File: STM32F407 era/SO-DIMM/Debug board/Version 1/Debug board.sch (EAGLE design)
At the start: 16 parts, among them J4 FTDI_DEVICE, J8 22-27-2021-02, X1 057-014-1, X2 BN35N61, X3 BN35N61, X4 BN35N61, X5 BN35N61, X6 BN35N61

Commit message: All board V1-RC1 done
all boards ready for inspection
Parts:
- added U$21: MICROFIT4, unicorn:MICROFIT4
- added U5, U6: (no value), connector:AUDIO-JACKPTH
- added X7, X8: BN35N61, con-coax:BN35N61
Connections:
- net CAN_N: now also U$21.PIN2, U5.LEFT, U6.LEFT, X7G$1.1
- net CAN_P: now also U$21.PIN1, U5.RIGHT, U6.RIGHT, X8G$1.1
- net GND: now also U$21.PIN3, U$21.PIN4, U5.SLEEVE, U6.SLEEVE, X7G$1.GND, X8G$1.GND
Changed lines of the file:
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@@
 <layer number="59" name="tCarbon" color="7" fill="1" visible="no" active="no"/>
 <layer number="60" name="bCarbon" color="7" fill="1" visible="no" active="no"/>
+<layer number="61" name="stand" color="7" fill="1" visible="no" active="no"/>
 <layer number="90" name="Modules" color="5" fill="1" visible="yes" active="yes"/>
 <layer number="91" name="Nets" color="2" fill="1" visible="yes" active="yes"/>
@@
 <layer number="128" name="_bValues" color="7" fill="1" visible="yes" active="yes"/>
 <layer number="129" name="Mask" color="7" fill="1" visible="yes" active="yes"/>
+<layer number="130" name="bLogo" color="7" fill="1" visible="yes" active="yes"/>
 <layer number="131" name="tAdjust" color="7" fill="1" visible="yes" active="yes"/>
 <layer number="132" name="bAdjust" color="7" fill="1" visible="yes" active="yes"/>
@@
 <part name="U$4" library="microbuilder" deviceset="12V" device=""/>
 <part name="GND10" library="supply1" deviceset="GND" device=""/>
+<part name="U5" library="connector" deviceset="AUDIO-JACK" device="PTH"/>
+<part name="U6" library="connector" deviceset="AUDIO-JACK" device="PTH"/>
+<part name="GND17" library="supply1" deviceset="GND" device=""/>
+<part name="U$21" library="unicorn" deviceset="MICROFIT4" device=""/>
+<part name="U$24" library="microbuilder" deviceset="GND" device=""/>
+<part name="X7" library="con-coax" deviceset="BN35N61" device=""/>
+<part name="X8" library="con-coax" deviceset="BN35N61" device=""/>
+<part name="GND11" library="supply1" deviceset="GND" device=""/>
+<part name="GND12" library="supply1" deviceset="GND" device=""/>
 </parts>
 <sheets>
@@
 <wire x1="96.52" y1="175.26" x2="96.52" y2="170.18" width="0.3048" layer="97"/>
 <wire x1="96.52" y1="170.18" x2="96.52" y2="134.62" width="0.3048" layer="97"/>
-<wire x1="96.52" y1="134.62" x2="160.02" y2="134.62" width="0.3048" layer="97"/>
-<wire x1="160.02" y1="134.62" x2="160.02" y2="175.26" width="0.3048" layer="97"/>
-<wire x1="160.02" y1="175.26" x2="132.08" y2="175.26" width="0.3048" layer="97"/>
+<wire x1="96.52" y1="134.62" x2="185.42" y2="134.62" width="0.3048" layer="97"/>
+<wire x1="185.42" y1="134.62" x2="185.42" y2="175.26" width="0.3048" layer="97"/>
+<wire x1="185.42" y1="175.26" x2="132.08" y2="175.26" width="0.3048" layer="97"/>
 <text x="99.06" y="172.72" size="1.778" layer="97" font="vector">BNC signal headers</text>
 <wire x1="132.08" y1="175.26" x2="96.52" y2="175.26" width="0.3048" layer="97"/>
@@
 <instance part="U$4" gate="G$1" x="114.3" y="119.38"/>
 <instance part="GND10" gate="1" x="114.3" y="104.14"/>
+<instance part="U5" gate="G$1" x="160.02" y="119.38"/>
+<instance part="U6" gate="G$1" x="160.02" y="111.76"/>
+<instance part="GND17" gate="1" x="167.64" y="104.14"/>
+<instance part="U$21" gate="G$1" x="177.8" y="91.44"/>
+<instance part="U$24" gate="G$1" x="167.64" y="83.82"/>
+<instance part="X7" gate="G$1" x="152.4" y="147.32" rot="MR0"/>
+<instance part="X8" gate="G$1" x="172.72" y="165.1" rot="MR0"/>
+<instance part="GND11" gate="1" x="147.32" y="139.7"/>
+<instance part="GND12" gate="1" x="167.64" y="157.48"/>
 </instances>
 <busses>
@@
 <wire x1="114.3" y1="109.22" x2="114.3" y2="106.68" width="0.1524" layer="91"/>
 </segment>
+<segment>
+<pinref part="U6" gate="G$1" pin="SLEEVE"/>
+<wire x1="165.1" y1="114.3" x2="167.64" y2="114.3" width="0.1524" layer="91"/>
+<wire x1="167.64" y1="114.3" x2="167.64" y2="106.68" width="0.1524" layer="91"/>
+<pinref part="U5" gate="G$1" pin="SLEEVE"/>
+<wire x1="165.1" y1="121.92" x2="167.64" y2="121.92" width="0.1524" layer="91"/>
+<wire x1="167.64" y1="121.92" x2="167.64" y2="114.3" width="0.1524" layer="91"/>
+<junction x="167.64" y="114.3"/>
+<pinref part="GND17" gate="1" pin="GND"/>
+</segment>
+<segment>
+<pinref part="U$21" gate="G$1" pin="PIN3"/>
+<pinref part="U$24" gate="G$1" pin="GND"/>
+<wire x1="170.18" y1="91.44" x2="167.64" y2="91.44" width="0.1524" layer="91"/>
+<wire x1="167.64" y1="91.44" x2="167.64" y2="88.9" width="0.1524" layer="91"/>
+<pinref part="U$21" gate="G$1" pin="PIN4"/>
+<wire x1="167.64" y1="88.9" x2="167.64" y2="86.36" width="0.1524" layer="91"/>
+<wire x1="170.18" y1="88.9" x2="167.64" y2="88.9" width="0.1524" layer="91"/>
+<junction x="167.64" y="88.9"/>
+</segment>
+<segment>
+<pinref part="X7" gate="G$1" pin="GND"/>
+<pinref part="GND11" gate="1" pin="GND"/>
+<wire x1="149.86" y1="144.78" x2="147.32" y2="144.78" width="0.1524" layer="91"/>
+<wire x1="147.32" y1="144.78" x2="147.32" y2="142.24" width="0.1524" layer="91"/>
+</segment>
+<segment>
+<pinref part="X8" gate="G$1" pin="GND"/>
+<pinref part="GND12" gate="1" pin="GND"/>
+<wire x1="170.18" y1="162.56" x2="167.64" y2="162.56" width="0.1524" layer="91"/>
+<wire x1="167.64" y1="162.56" x2="167.64" y2="160.02" width="0.1524" layer="91"/>
+</segment>
 </net>
 <net name="3.3V" class="0">
@@
 <label x="81.28" y="109.22" size="1.27" layer="95" rot="R180" xref="yes"/>
 </segment>
+<segment>
+<pinref part="U6" gate="G$1" pin="RIGHT"/>
+<wire x1="165.1" y1="111.76" x2="170.18" y2="111.76" width="0.1524" layer="91"/>
+<pinref part="U5" gate="G$1" pin="RIGHT"/>
+<wire x1="165.1" y1="119.38" x2="170.18" y2="119.38" width="0.1524" layer="91"/>
+<wire x1="170.18" y1="119.38" x2="175.26" y2="119.38" width="0.1524" layer="91"/>
+<wire x1="170.18" y1="111.76" x2="170.18" y2="119.38" width="0.1524" layer="91"/>
+<junction x="170.18" y="119.38"/>
+<label x="175.26" y="119.38" size="1.27" layer="95" xref="yes"/>
+</segment>
+<segment>
+<pinref part="U$21" gate="G$1" pin="PIN1"/>
+<wire x1="170.18" y1="96.52" x2="167.64" y2="96.52" width="0.1524" layer="91"/>
+<label x="167.64" y="96.52" size="1.27" layer="95" rot="R180" xref="yes"/>
+</segment>
+<segment>
+<pinref part="X8" gate="G$1" pin="1"/>
+<wire x1="167.64" y1="165.1" x2="170.18" y2="165.1" width="0.1524" layer="91"/>
+<label x="167.64" y="165.1" size="1.27" layer="95" rot="R180" xref="yes"/>
+</segment>
 </net>
 <net name="CAN_N" class="0">
@@
 <label x="81.28" y="119.38" size="1.27" layer="95" rot="R180" xref="yes"/>
 </segment>
+<segment>
+<pinref part="U6" gate="G$1" pin="LEFT"/>
+<wire x1="165.1" y1="109.22" x2="172.72" y2="109.22" width="0.1524" layer="91"/>
+<pinref part="U5" gate="G$1" pin="LEFT"/>
+<wire x1="165.1" y1="116.84" x2="172.72" y2="116.84" width="0.1524" layer="91"/>
+<wire x1="172.72" y1="116.84" x2="175.26" y2="116.84" width="0.1524" layer="91"/>
+<wire x1="172.72" y1="109.22" x2="172.72" y2="116.84" width="0.1524" layer="91"/>
+<junction x="172.72" y="116.84"/>
+<label x="175.26" y="116.84" size="1.27" layer="95" xref="yes"/>
+</segment>
+<segment>
+<pinref part="U$21" gate="G$1" pin="PIN2"/>
+<wire x1="170.18" y1="93.98" x2="167.64" y2="93.98" width="0.1524" layer="91"/>
+<label x="167.64" y="93.98" size="1.27" layer="95" rot="R180" xref="yes"/>
+</segment>
+<segment>
+<pinref part="X7" gate="G$1" pin="1"/>
+<wire x1="147.32" y1="147.32" x2="149.86" y2="147.32" width="0.1524" layer="91"/>
+<label x="147.32" y="147.32" size="1.27" layer="95" rot="R180" xref="yes"/>
+</segment>
 </net>

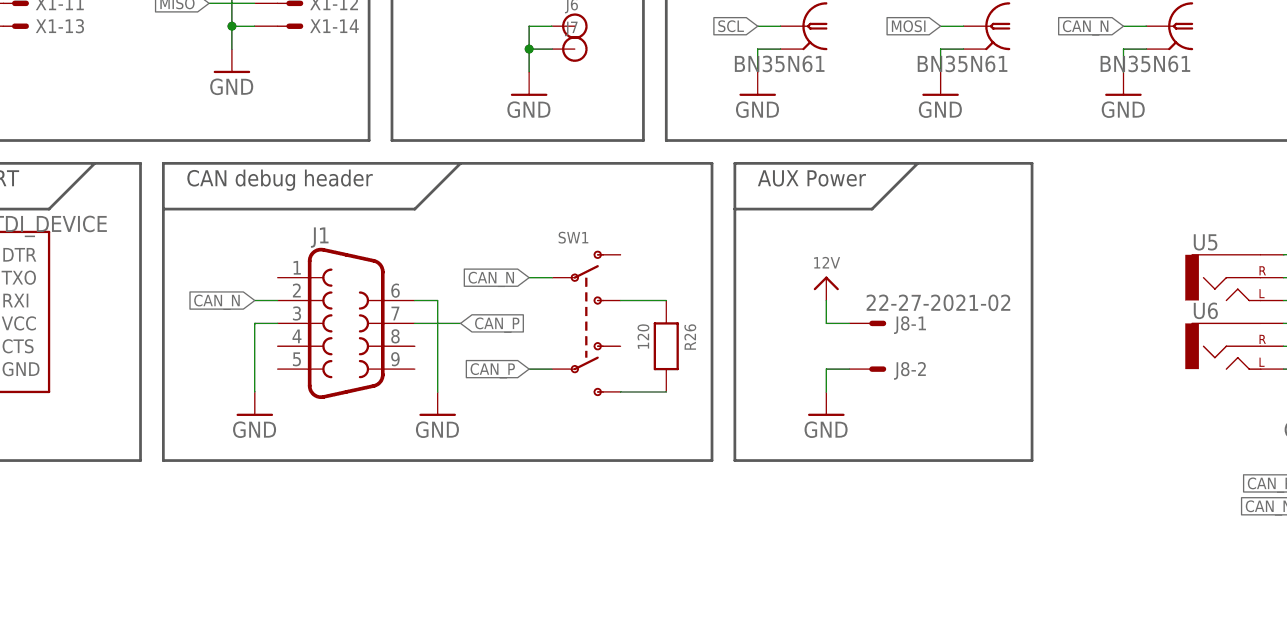
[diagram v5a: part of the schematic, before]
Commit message: last end changes on boards
Dev board
- Added 8 LED for ekstra debugging feature
- fixed Tvalue silkscreen
-

COM/TC
- fixed connections om P-channel RPP
- 12V from debug changed to include RPP and fuse

Dash
- fixed connections om P-channel RPP
- 12V from debug changed to include RPP and fuse

debug
- Added "ohm/not ohm to silkscreen
- Added BNC connectors for CAN

and much much more
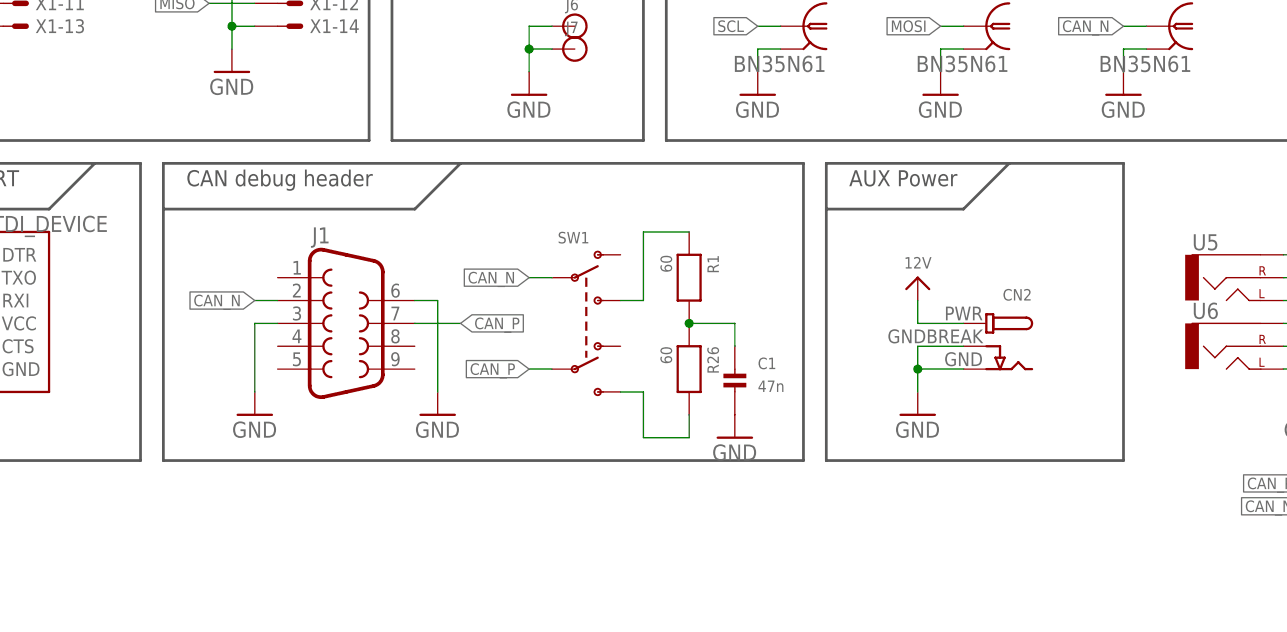
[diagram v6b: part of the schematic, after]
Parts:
- removed J8: 22-27-2021-02, con-molex:22-27-2021-02
- added C1: 47n, microbuilder:CAP_CERAMIC_0603
- added CN2: (no value), microbuilder:DCBARRELPTH
- added R1: 60, microbuilder:RESISTOR_0603
- R26: value 120 -> 60
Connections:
- removed net N$8: R26.1, SW1.S1
- new net N$1: C1.P$1, R1.2, R26.1
- new net N$2: R1.1, SW1.S1
- net 12V: now also CN2.PWR; no longer J8-1.S
- net GND: now also C1.P$2, CN2.GND, CN2.GNDBREAK; no longer J8-2.S
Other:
- moved on the sheet: R26
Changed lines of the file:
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@@
 <part name="GND7" library="supply1" deviceset="GND" device=""/>
 <part name="SW1" library="microbuilder" deviceset="SWITCH_DPDT" device=""/>
-<part name="R26" library="microbuilder" deviceset="RESISTOR" device="_0603" value="120"/>
+<part name="R26" library="microbuilder" deviceset="RESISTOR" device="_0603" value="60"/>
 <part name="X2" library="con-coax" deviceset="BN35N61" device=""/>
 <part name="X3" library="con-coax" deviceset="BN35N61" device=""/>
@@
 <part name="J7" library="SparkFun-Connectors" deviceset="BANANA_CONN" device=""/>
 <part name="FRAME1" library="SparkFun-Aesthetics" deviceset="FRAME-A4L" device=""/>
-<part name="J8" library="con-molex" deviceset="22-?-02" device="27-2021"/>
 <part name="U$4" library="microbuilder" deviceset="12V" device=""/>
 <part name="GND10" library="supply1" deviceset="GND" device=""/>
@@
 <part name="GND11" library="supply1" deviceset="GND" device=""/>
 <part name="GND12" library="supply1" deviceset="GND" device=""/>
+<part name="R1" library="microbuilder" deviceset="RESISTOR" device="_0603" value="60"/>
+<part name="C1" library="microbuilder" deviceset="CAP_CERAMIC" device="_0603" value="47n"/>
+<part name="GND13" library="supply1" deviceset="GND" device=""/>
+<part name="CN2" library="microbuilder" deviceset="DCBARREL" device="PTH"/>
 </parts>
 <sheets>
@@
 <wire x1="40.64" y1="132.08" x2="40.64" y2="127" width="0.3048" layer="97"/>
 <wire x1="40.64" y1="127" x2="40.64" y2="99.06" width="0.3048" layer="97"/>
-<wire x1="40.64" y1="99.06" x2="101.6" y2="99.06" width="0.3048" layer="97"/>
-<wire x1="101.6" y1="99.06" x2="101.6" y2="132.08" width="0.3048" layer="97"/>
-<wire x1="101.6" y1="132.08" x2="73.66" y2="132.08" width="0.3048" layer="97"/>
+<wire x1="40.64" y1="99.06" x2="111.76" y2="99.06" width="0.3048" layer="97"/>
+<wire x1="111.76" y1="99.06" x2="111.76" y2="132.08" width="0.3048" layer="97"/>
+<wire x1="111.76" y1="132.08" x2="73.66" y2="132.08" width="0.3048" layer="97"/>
 <text x="43.18" y="129.54" size="1.778" layer="97" font="vector">CAN debug header</text>
 <wire x1="73.66" y1="132.08" x2="40.64" y2="132.08" width="0.3048" layer="97"/>
@@
 <wire x1="96.52" y1="170.18" x2="127" y2="170.18" width="0.3048" layer="97"/>
 <wire x1="127" y1="170.18" x2="132.08" y2="175.26" width="0.3048" layer="97"/>
-<wire x1="104.14" y1="132.08" x2="124.46" y2="132.08" width="0.3048" layer="97"/>
-<wire x1="124.46" y1="132.08" x2="137.16" y2="132.08" width="0.3048" layer="97"/>
-<wire x1="137.16" y1="132.08" x2="137.16" y2="99.06" width="0.3048" layer="97"/>
-<wire x1="137.16" y1="99.06" x2="104.14" y2="99.06" width="0.3048" layer="97"/>
-<wire x1="104.14" y1="99.06" x2="104.14" y2="127" width="0.3048" layer="97"/>
-<text x="106.68" y="129.54" size="1.778" layer="97" font="vector">AUX Power</text>
-<wire x1="104.14" y1="127" x2="104.14" y2="132.08" width="0.3048" layer="97"/>
-<wire x1="104.14" y1="127" x2="119.38" y2="127" width="0.3048" layer="97"/>
-<wire x1="119.38" y1="127" x2="124.46" y2="132.08" width="0.3048" layer="97"/>
+<wire x1="114.3" y1="132.08" x2="134.62" y2="132.08" width="0.3048" layer="97"/>
+<wire x1="134.62" y1="132.08" x2="147.32" y2="132.08" width="0.3048" layer="97"/>
+<wire x1="147.32" y1="132.08" x2="147.32" y2="99.06" width="0.3048" layer="97"/>
+<wire x1="147.32" y1="99.06" x2="114.3" y2="99.06" width="0.3048" layer="97"/>
+<wire x1="114.3" y1="99.06" x2="114.3" y2="127" width="0.3048" layer="97"/>
+<text x="116.84" y="129.54" size="1.778" layer="97" font="vector">AUX Power</text>
+<wire x1="114.3" y1="127" x2="114.3" y2="132.08" width="0.3048" layer="97"/>
+<wire x1="114.3" y1="127" x2="129.54" y2="127" width="0.3048" layer="97"/>
+<wire x1="129.54" y1="127" x2="134.62" y2="132.08" width="0.3048" layer="97"/>
 </plain>
 <instances>
@@
 <instance part="GND7" gate="1" x="71.12" y="104.14"/>
 <instance part="SW1" gate="G$1" x="88.9" y="114.3"/>
-<instance part="R26" gate="G$1" x="96.52" y="111.76" rot="R270"/>
+<instance part="R26" gate="G$1" x="99.06" y="109.22" rot="R270"/>
 <instance part="X2" gate="G$1" x="111.76" y="165.1" rot="MR0"/>
 <instance part="X3" gate="G$1" x="132.08" y="165.1" rot="MR0"/>
@@
 <instance part="J7" gate="G$1" x="86.36" y="144.78"/>
 <instance part="FRAME1" gate="G$1" x="0" y="0"/>
-<instance part="J8" gate="-1" x="119.38" y="114.3"/>
-<instance part="J8" gate="-2" x="119.38" y="109.22"/>
-<instance part="U$4" gate="G$1" x="114.3" y="119.38"/>
-<instance part="GND10" gate="1" x="114.3" y="104.14"/>
+<instance part="U$4" gate="G$1" x="124.46" y="119.38"/>
+<instance part="GND10" gate="1" x="124.46" y="104.14"/>
 <instance part="U5" gate="G$1" x="160.02" y="119.38"/>
 <instance part="U6" gate="G$1" x="160.02" y="111.76"/>
@@
 <instance part="GND11" gate="1" x="147.32" y="139.7"/>
 <instance part="GND12" gate="1" x="167.64" y="157.48"/>
+<instance part="R1" gate="G$1" x="99.06" y="119.38" rot="R270"/>
+<instance part="C1" gate="G$1" x="104.14" y="106.68"/>
+<instance part="GND13" gate="1" x="104.14" y="101.6"/>
+<instance part="CN2" gate="G$1" x="132.08" y="111.76" rot="MR0"/>
 </instances>
 <busses>
@@
 </segment>
 <segment>
-<pinref part="J8" gate="-2" pin="S"/>
 <pinref part="GND10" gate="1" pin="GND"/>
-<wire x1="116.84" y1="109.22" x2="114.3" y2="109.22" width="0.1524" layer="91"/>
-<wire x1="114.3" y1="109.22" x2="114.3" y2="106.68" width="0.1524" layer="91"/>
+<wire x1="129.54" y1="109.22" x2="124.46" y2="109.22" width="0.1524" layer="91"/>
+<wire x1="124.46" y1="109.22" x2="124.46" y2="106.68" width="0.1524" layer="91"/>
+<pinref part="CN2" gate="G$1" pin="GND"/>
+<pinref part="CN2" gate="G$1" pin="GNDBREAK"/>
+<wire x1="129.54" y1="111.76" x2="124.46" y2="111.76" width="0.1524" layer="91"/>
+<wire x1="124.46" y1="111.76" x2="124.46" y2="109.22" width="0.1524" layer="91"/>
+<junction x="124.46" y="109.22"/>
 </segment>
 <segment>
@@
 <wire x1="167.64" y1="162.56" x2="167.64" y2="160.02" width="0.1524" layer="91"/>
 </segment>
+<segment>
+<pinref part="C1" gate="G$1" pin="P$2"/>
+<pinref part="GND13" gate="1" pin="GND"/>
+</segment>
 </net>
 <net name="3.3V" class="0">
@@
 </segment>
 <segment>
-<pinref part="J8" gate="-1" pin="S"/>
 <pinref part="U$4" gate="G$1" pin="12V"/>
-<wire x1="116.84" y1="114.3" x2="114.3" y2="114.3" width="0.1524" layer="91"/>
-<wire x1="114.3" y1="114.3" x2="114.3" y2="116.84" width="0.1524" layer="91"/>
+<wire x1="129.54" y1="114.3" x2="124.46" y2="114.3" width="0.1524" layer="91"/>
+<wire x1="124.46" y1="114.3" x2="124.46" y2="116.84" width="0.1524" layer="91"/>
+<pinref part="CN2" gate="G$1" pin="PWR"/>
 </segment>
 </net>
@@
 <pinref part="SW1" gate="G$1" pin="S2"/>
 <pinref part="R26" gate="G$1" pin="2"/>
-<wire x1="91.44" y1="106.68" x2="96.52" y2="106.68" width="0.1524" layer="91"/>
-</segment>
-</net>
-<net name="N$8" class="0">
-<segment>
+<wire x1="91.44" y1="106.68" x2="93.98" y2="106.68" width="0.1524" layer="91"/>
+<wire x1="93.98" y1="106.68" x2="93.98" y2="101.6" width="0.1524" layer="91"/>
+<wire x1="93.98" y1="101.6" x2="99.06" y2="101.6" width="0.1524" layer="91"/>
+<wire x1="99.06" y1="101.6" x2="99.06" y2="104.14" width="0.1524" layer="91"/>
+</segment>
+</net>
+<net name="N$1" class="0">
+<segment>
+<pinref part="R26" gate="G$1" pin="1"/>
+<pinref part="R1" gate="G$1" pin="2"/>
+<pinref part="C1" gate="G$1" pin="P$1"/>
+<wire x1="99.06" y1="114.3" x2="104.14" y2="114.3" width="0.1524" layer="91"/>
+<wire x1="104.14" y1="114.3" x2="104.14" y2="111.76" width="0.1524" layer="91"/>
+<junction x="99.06" y="114.3"/>
+</segment>
+</net>
+<net name="N$2" class="0">
+<segment>
+<pinref part="R1" gate="G$1" pin="1"/>
+<wire x1="99.06" y1="124.46" x2="93.98" y2="124.46" width="0.1524" layer="91"/>
+<wire x1="93.98" y1="124.46" x2="93.98" y2="116.84" width="0.1524" layer="91"/>
 <pinref part="SW1" gate="G$1" pin="S1"/>
-<pinref part="R26" gate="G$1" pin="1"/>
-<wire x1="91.44" y1="116.84" x2="96.52" y2="116.84" width="0.1524" layer="91"/>
-</segment>
-</net>
+<wire x1="93.98" y1="116.84" x2="91.44" y2="116.84" width="0.1524" layer="91"/>
+</segment>
+</net>
